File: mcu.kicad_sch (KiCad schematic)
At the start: 17 parts, among them IC3 ATSAMD21G18A-MFT, IC5 AD7298BCPZ, J1 FTSH-105-01-L-DV-K

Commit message: Initial layout
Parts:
- removed C25, C6: 0.1uF, symbol Device:C_Small
- removed C5, C7: 10uF, symbol Device:C_Small
- removed IC5: AD7298BCPZ, BLDC-Motor-Driver:AD7298, symbol BLDC-Motor-Driver_v2:AD7298BCPZ
- R19, R6: footprint (none) -> Resistor_SMD:R_0603_1608Metric
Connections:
- net SERCOM1_PAD1 is gone; now on net SERCOM3_PAD1: IC3.26 (PA17)
- net SERCOM1_PAD2 is gone; now on net SERCOM3_PAD2: IC3.27 (PA18)
- net BENCHMARK_IO_1: now also IC3.37 (PB22); no longer IC3.10 (PA05)
- net BENCHMARK_IO_2: now also IC3.38 (PB23); no longer IC3.11 (PA06)
- net BENCHMARK_IO_3: now also IC3.39 (PA27); no longer IC3.12 (PA07)
- net SERCOM3_PAD1: no longer IC3.32 (PA23)
- net SERCOM3_PAD2: no longer IC3.33 (PA24)
- net VDDANA: now also IC3.6 (VDDANA)
- net SERCOM4_PAD1: now reaches IC3.22 (PA13)
- net ADC_VREFA: now reaches IC3.4 (PA03)
- net ADC_AIN4: now reaches IC3.9 (PA04)
- net SERCOM3_PAD0 renamed SERCOM5_PAD0
- net SERCOM3_PAD3 renamed SERCOM5_PAD3
- net XIN renamed SERCOM4_PAD2
- net XIN32: no longer names the net of IC3.1 (PA00)
- net XOUT: no longer names the net of IC3.24 (PA15)
- net XOUT32: no longer names the net of IC3.2 (PA01)
- new net ADC_AIN5: IC3.10 (PA05)
- new net ADC_AIN6: IC3.11 (PA06)
- new net SERCOM5_PAD1: IC3.32 (PA23)
- new net SERCOM5_PAD2: IC3.33 (PA24)
- no-connect marks 27 -> 19

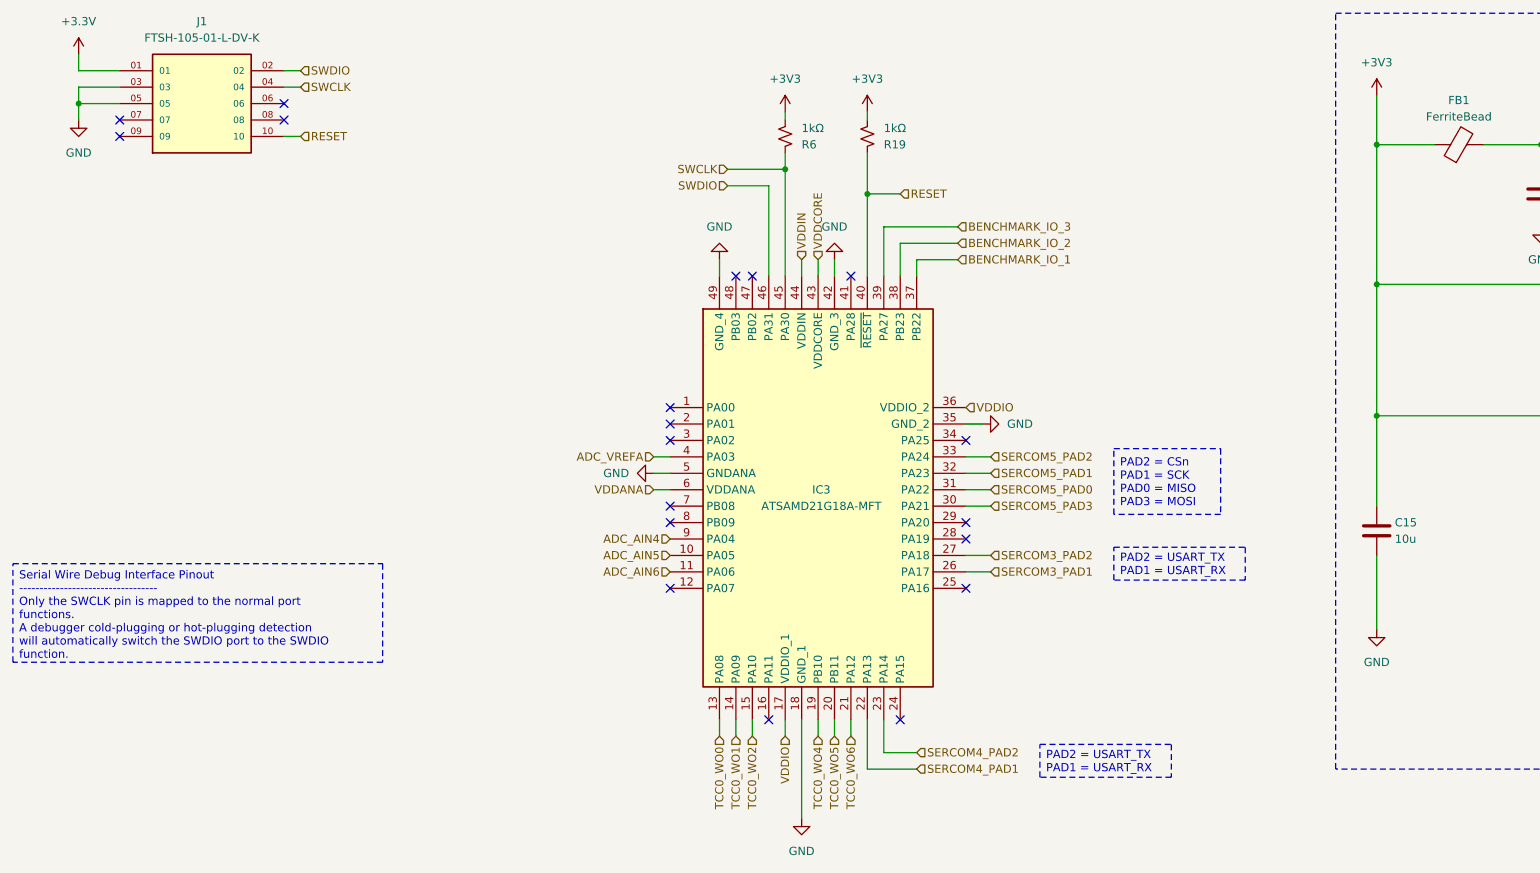
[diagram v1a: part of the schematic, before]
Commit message: Almost all routing done
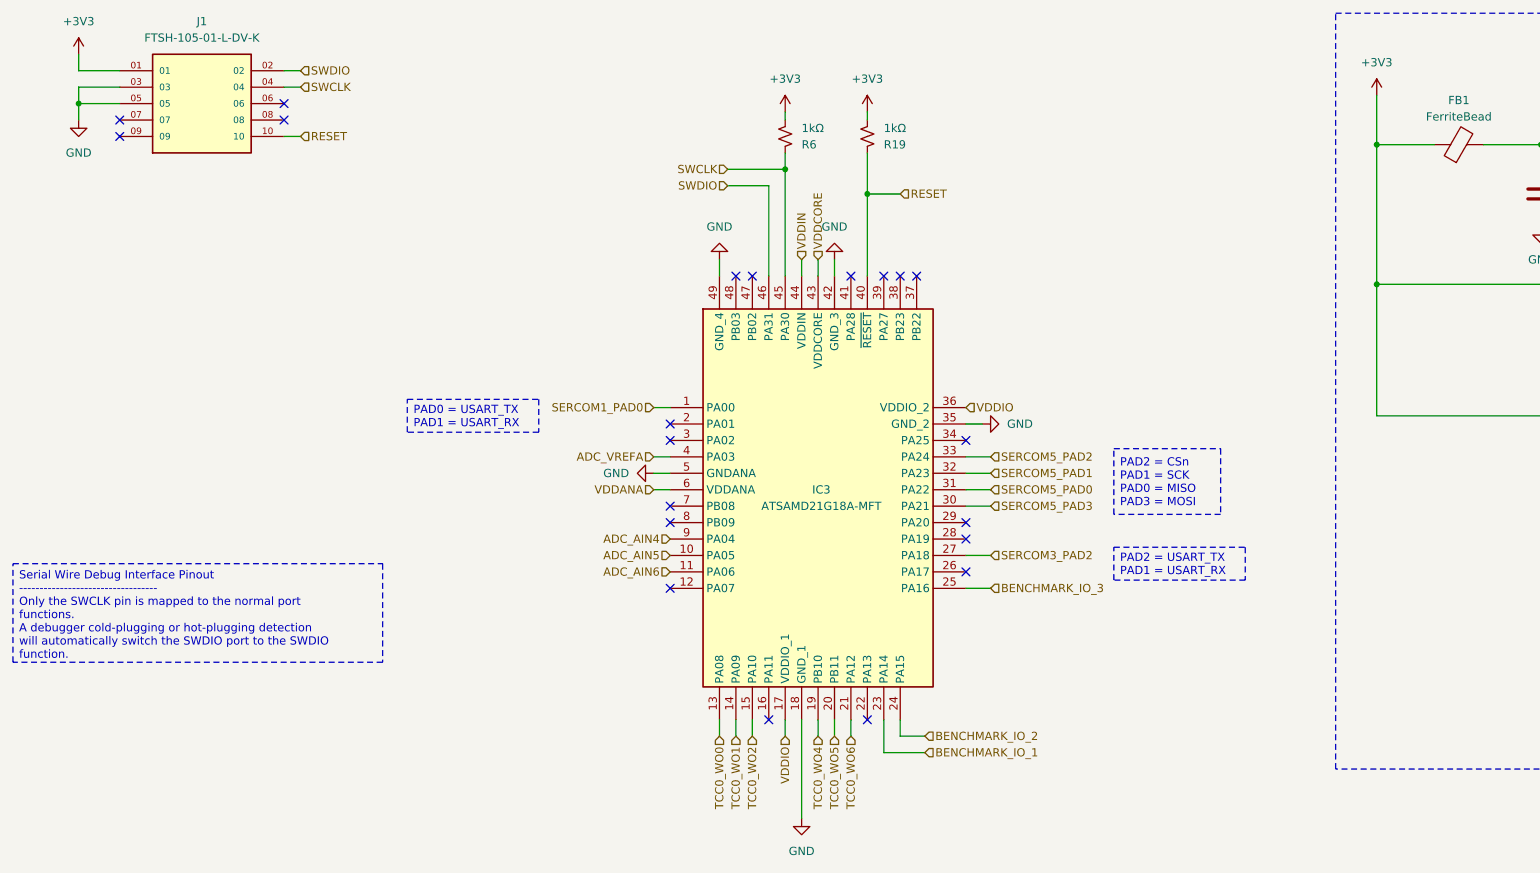
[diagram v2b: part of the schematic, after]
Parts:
- removed C15: 10u, Capacitor_SMD:C_0603_1608Metric, symbol Device:C
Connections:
- net +3.3V is gone; now on net +3V3: J1.01
- net SERCOM4_PAD2 is gone; now on net BENCHMARK_IO_1: IC3.23 (PA14)
- net BENCHMARK_IO_1: no longer IC3.37 (PB22)
- net BENCHMARK_IO_2: now also IC3.24 (PA15); no longer IC3.38 (PB23)
- net BENCHMARK_IO_3: now also IC3.25 (PA16); no longer IC3.39 (PA27)
- net SERCOM1_PAD0: now reaches IC3.1 (PA00)
- net SERCOM3_PAD1: no longer names the net of IC3.26 (PA17)
- net SERCOM4_PAD1: no longer names the net of IC3.22 (PA13)
- no-connect marks 19 -> 21

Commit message: More routing
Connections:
- net SERCOM4_PAD0: now reaches IC3.7 (PB08)
- net SERCOM3_PAD2: no longer names the net of IC3.27 (PA18)
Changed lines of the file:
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@@
 		)
 	)
-	(text_box "PAD2 = USART_TX\nPAD1 = USART_RX"
-		(exclude_from_sim no)
-		(at 186.69 99.06 0)
-		(size 20.32 5.08)
-		(margins 0.9525 0.9525 0.9525 0.9525)
-		(stroke
-			(width 0)
-			(type dash)
-		)
-		(fill
-			(type none)
-		)
-		(effects
-			(font
-				(size 1.27 1.27)
-			)
-			(justify left)
-		)
-	)
 	(text_box "Power Supplies\n---------------\nThe device has several different power supply pins:\n• VDDIO: Powers I/O lines, OSC8M and XOSC. Voltage is 1.62V to 3.63V.\n• VDDIN: Powers I/O lines and the internal regulator. Voltage is 1.62V to 3.63V.\n• VDDANA: Powers I/O lines and the ADC, AC, DAC, PTC, OSCULP32K, OSC32K, XOSC32K. Voltage is\n1.62V to 3.63V.\n• VDDCORE: Internal regulated voltage output. Powers the core, memories, peripherals,\nFDPLL96M, and DFLL48M. Voltage is 1.2V.\nThe same voltage must be applied to both VDDIN, VDDIO and VDDANA. This common voltage is\nreferred to as VDD in the datasheet.\nThe ground pins, GND, are common to VDDCORE, VDDIO and VDDIN. The ground pin for VDDANA is\nGNDANA."
 		(exclude_from_sim no)
@@
 	)
 	(no_connect
+		(at 163.83 100.33)
+	)
+	(no_connect
 		(at 153.67 57.15)
 	)
@@
 		(at 118.11 105.41)
 	)
-	(no_connect
-		(at 118.11 92.71)
-	)
 	(wire
 		(pts
@@
 	(wire
 		(pts
-			(xy 167.64 100.33) (xy 163.83 100.33)
+			(xy 148.59 31.75) (xy 148.59 33.02)
 		)
 		(stroke
@@
 	(wire
 		(pts
-			(xy 148.59 31.75) (xy 148.59 33.02)
+			(xy 60.96 27.94) (xy 58.42 27.94)
 		)
 		(stroke
@@
 	(wire
 		(pts
-			(xy 60.96 27.94) (xy 58.42 27.94)
+			(xy 135.89 31.75) (xy 135.89 33.02)
 		)
 		(stroke
@@
 	(wire
 		(pts
-			(xy 135.89 31.75) (xy 135.89 33.02)
+			(xy 167.64 92.71) (xy 163.83 92.71)
 		)
 		(stroke
@@
 	(wire
 		(pts
-			(xy 167.64 92.71) (xy 163.83 92.71)
+			(xy 288.29 58.42) (xy 276.86 58.42)
 		)
 		(stroke
@@
 	(wire
 		(pts
-			(xy 288.29 58.42) (xy 276.86 58.42)
+			(xy 252.73 40.64) (xy 252.73 36.83)
 		)
 		(stroke
@@
 	(wire
 		(pts
-			(xy 252.73 40.64) (xy 252.73 36.83)
+			(xy 26.67 27.94) (xy 33.02 27.94)
 		)
 		(stroke
@@
 	(wire
 		(pts
-			(xy 26.67 27.94) (xy 33.02 27.94)
+			(xy 115.57 92.71) (xy 118.11 92.71)
 		)
 		(stroke
@@
 		)
 	)
+	(hierarchical_label "SERCOM4_PAD0"
+		(shape input)
+		(at 115.57 92.71 180)
+		(effects
+			(font
+				(size 1.27 1.27)
+			)
+			(justify right)
+		)
+	)
 	(hierarchical_label "SWCLK"
 		(shape input)
@@
 		(effects
 			(font
-				(size 1.27 1.27)
-			)
-			(justify left)
-		)
-	)
-	(hierarchical_label "SERCOM3_PAD2"
-		(shape input)
-		(at 167.64 100.33 0)
-		(effects
-			(font
